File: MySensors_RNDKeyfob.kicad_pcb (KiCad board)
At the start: 2 copper layers, 27 x 42.9 mm, 25 parts, among them J1 CONN_01X02, P1 CONN_01X01, P2 CONN_02X03, SW1 SW_SPST, SW2 SW_SPST, SW3 SW_SPST, SW4 SW_SPST, SW5 SW_SPST, U1 ATSHA204A, U2 RFM69HCW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

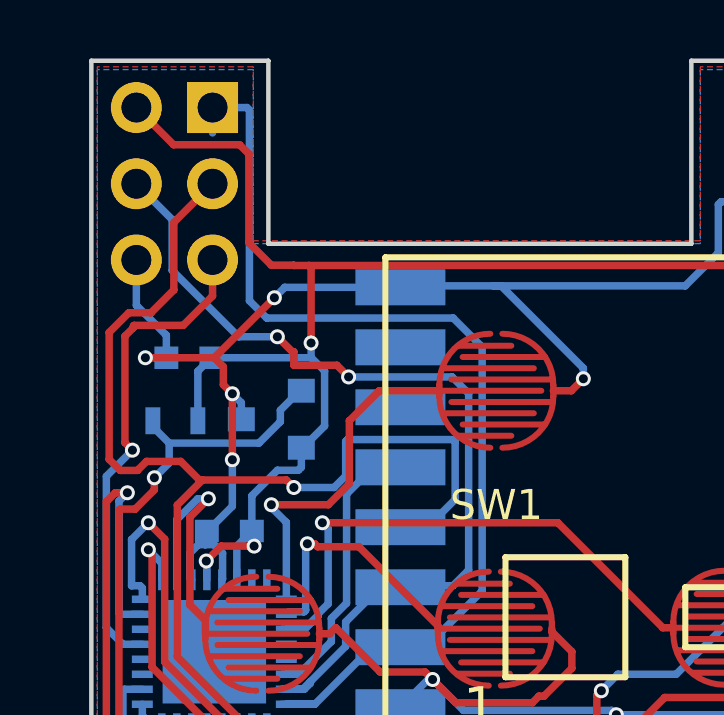
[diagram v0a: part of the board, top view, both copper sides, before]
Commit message: Added pull-up to CS line to stablize ICSP programming
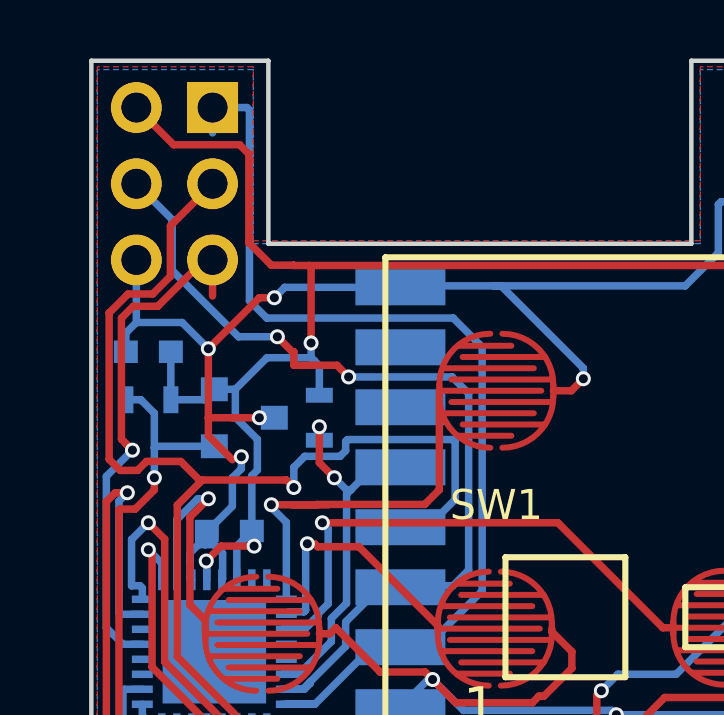
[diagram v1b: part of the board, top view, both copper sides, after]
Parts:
- added R5: R, Resistors_SMD:R_0603, B.Cu at (194.1, 69.0)
- moved C2 1.36 mm to (188.4, 66.8)
- moved R1 1.14 mm to (188.4, 68.4)
- moved U1 0.90 mm to (191.6, 69.0), turned to 0 degrees
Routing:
- net /A3: track 20.7 -> 18.5 mm
- net /D5: track 11.8 -> 13.7 mm
- net /RESET: track 16.3 -> 17.7 mm
- net GND: track 175.1 -> 176.1 mm
- net /D10: track 12.7 -> 12.9 mm, vias 0 -> 2
